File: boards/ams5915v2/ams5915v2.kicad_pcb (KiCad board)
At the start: 2 copper layers, 17.8 x 53.3 mm, 17 parts, among them J1 Conn_01x04, U1 MAX4995A, U2 TLV73333PDBVR, U3 AMS5915, U4 AMS5915

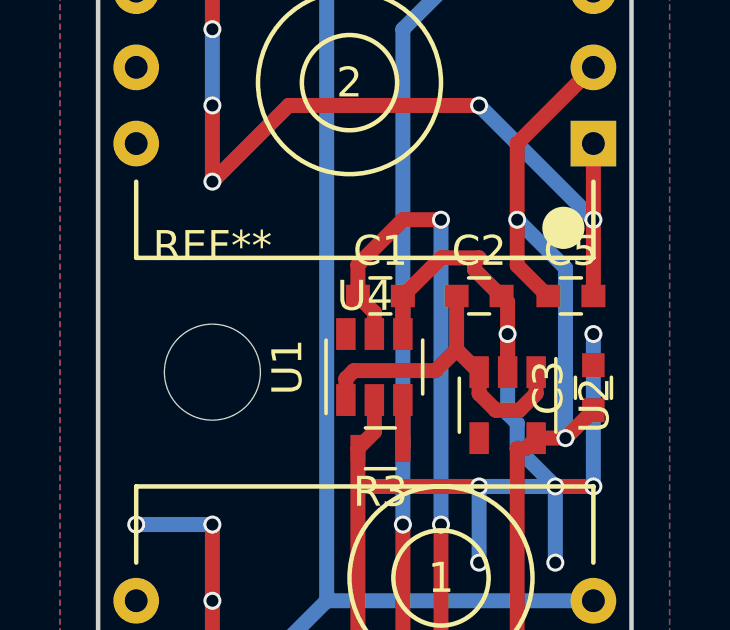
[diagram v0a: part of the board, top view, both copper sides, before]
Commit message: ams5915v2: fixed permanently off max4995
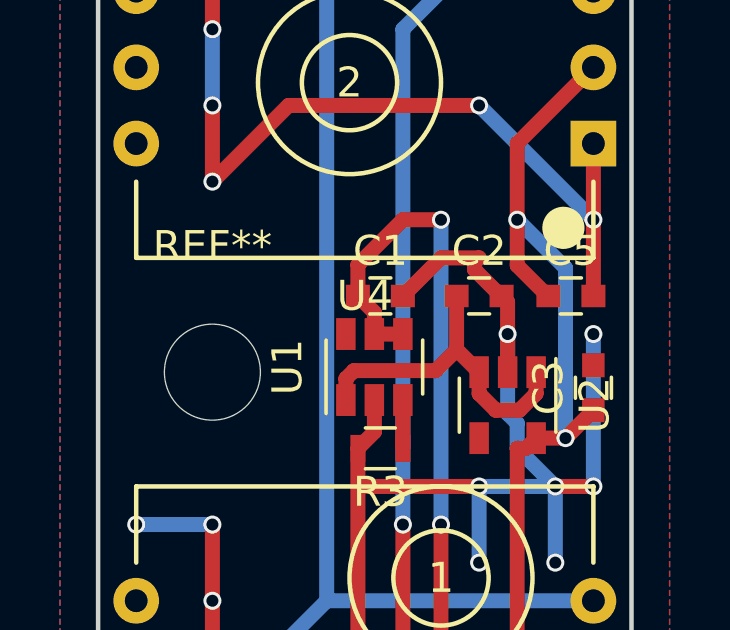
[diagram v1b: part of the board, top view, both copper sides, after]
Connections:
- U1 pad 4: /GND -> /5v
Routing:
- net /GND: track 156.6 -> 155.3 mm
- net /5v: track 36.2 -> 37.1 mm
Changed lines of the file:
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@@
       (net 7 "Net-(R3-Pad1)"))
     (pad 4 smd rect (at 1.1 0.95 90) (size 1.06 0.65) (layers F.Cu F.Paste F.Mask)
-      (net 1 /GND))
+      (net 2 /5v))
     (pad 6 smd rect (at 1.1 -0.95 90) (size 1.06 0.65) (layers F.Cu F.Paste F.Mask)
       (net 8 "Net-(U1-Pad6)"))
@@
   (segment (start 157.33 81.675) (end 158.205 82.55) (width 0.5) (layer F.Cu) (net 1))
   (segment (start 158.205 82.55) (end 158.23 82.55) (width 0.5) (layer F.Cu) (net 1))
-  (segment (start 154.94 82.55) (end 154.94 83.82) (width 0.5) (layer F.Cu) (net 1))
   (segment (start 152.4 95.25) (end 153.67 96.52) (width 0.5) (layer B.Cu) (net 1))
   (segment (start 153.67 96.52) (end 158.75 96.52) (width 0.5) (layer B.Cu) (net 1))
@@
   (segment (start 153.44 87.63) (end 153.99 87.08) (width 0.5) (layer F.Cu) (net 1))
   (segment (start 153.99 87.08) (end 153.99 86.02) (width 0.5) (layer F.Cu) (net 1))
+  (segment (start 153.99 83.82) (end 154.94 83.82) (width 0.5) (layer F.Cu) (net 2))
   (segment (start 156.21 80.01) (end 154.94 80.01) (width 0.5) (layer F.Cu) (net 2))
   (segment (start 154.94 80.01) (end 153.44 81.51) (width 0.5) (layer F.Cu) (net 2))

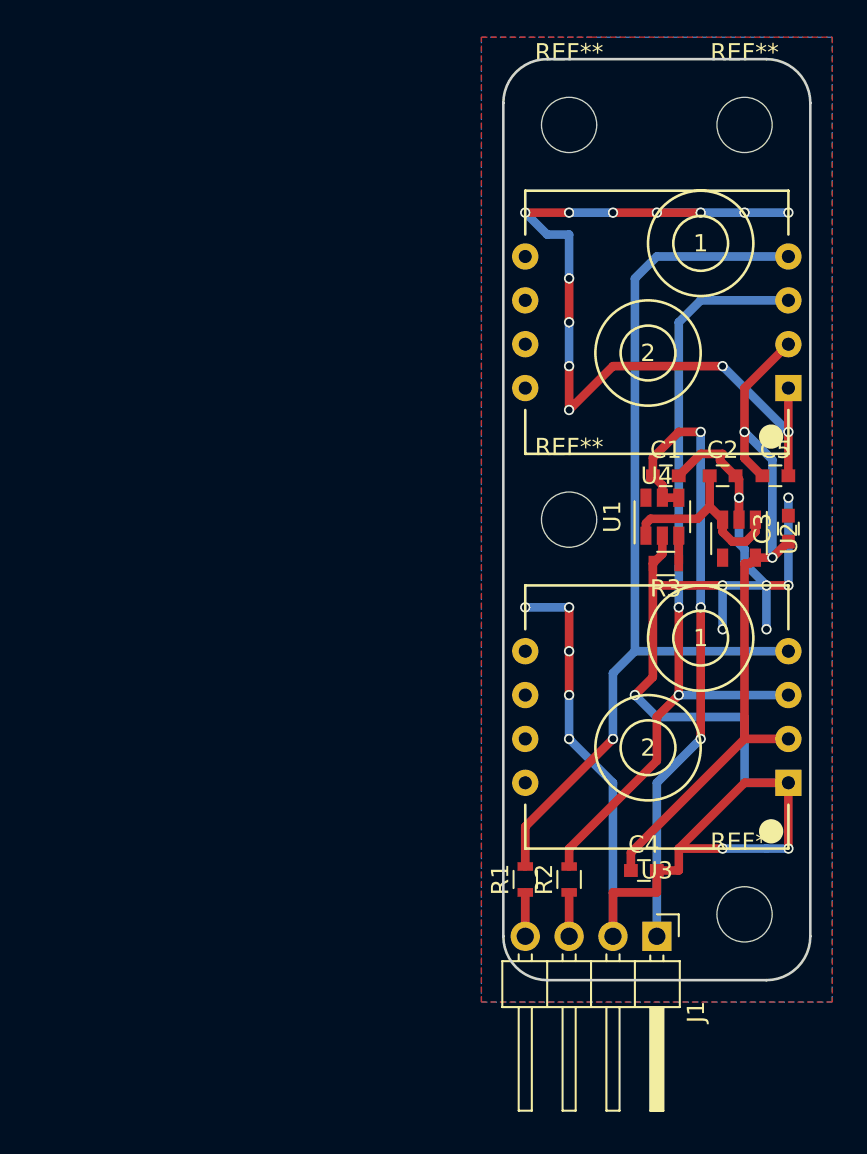
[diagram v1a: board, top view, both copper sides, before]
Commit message: ams5915x2: complete redesign. using leds to signal power, fault and 3v3. added pullup on fault line, fixed missing libs, fixed believed short
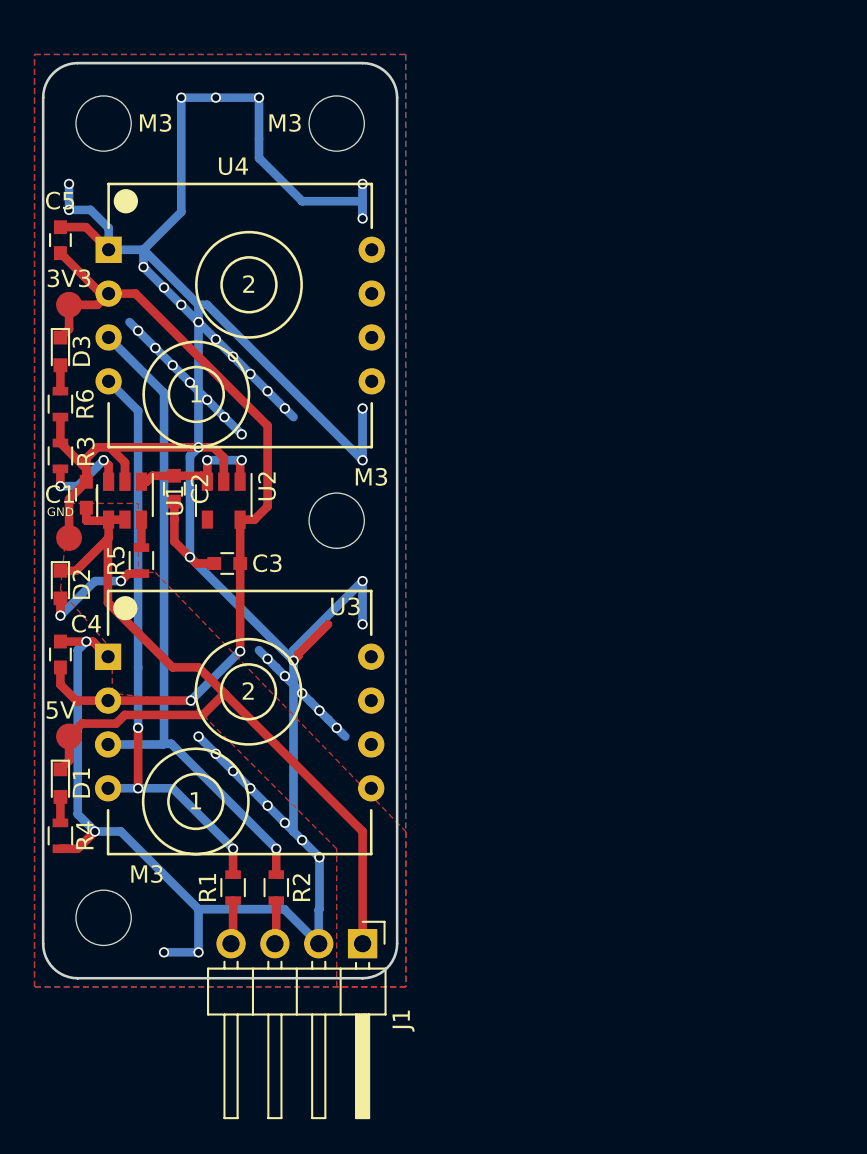
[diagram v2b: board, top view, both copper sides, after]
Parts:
- added 3V3: 3v3, Measurement_Points:Measurement_Point_Round-SMD-Pad_Small, F.Cu at (119.6, 72.7)
- added 5V: 5v, Measurement_Points:Measurement_Point_Round-SMD-Pad_Small, F.Cu at (119.6, 97.7)
- added D1: LED, LEDs:LED_0603, F.Cu at (119.1, 100.3)
- added D2: LED, LEDs:LED_0603, F.Cu at (119.1, 88.8)
- added D3: LED, LEDs:LED_0603, F.Cu at (119.1, 75.3)
- added GND: GND, Measurement_Points:Measurement_Point_Round-SMD-Pad_Small, F.Cu at (119.6, 86.2)
- added R4: R, Resistors_SMD:R_0603, F.Cu at (119.1, 103.4)
- added R5: R, Resistors_SMD:R_0603, F.Cu at (123.8, 87.5)
- added R6: R, Resistors_SMD:R_0603, F.Cu at (119.1, 78.4)
- moved C5 43.6 mm to (119.1, 68.9), turned to 90 degrees
- moved U4 42.4 mm to (121.9, 65.7), turned to 270 degrees
- moved U3 42.1 mm to (121.9, 89.2), turned to 270 degrees
- moved M3 37.1 mm to (121.6, 108.2)
- moved C4 36.0 mm to (119.1, 92.9), turned to 90 degrees
- moved R3 35.6 mm to (119.1, 81.4), turned to 90 degrees
- moved C1 33.6 mm to (120.6, 83.7), turned to 90 degrees
- moved C3 32.6 mm to (128.8, 87.6), turned to 180 degrees
- moved C2 31.8 mm to (125.7, 83.3), turned to 270 degrees
- moved U1 31.1 mm to (122.9, 84.0), turned to 270 degrees
- moved U2 29.9 mm to (128.6, 84.0)
- moved M3 27.0 mm to (121.6, 62.1)
- moved M3 23.6 mm to (135.1, 62.1)
- moved J1 17.0 mm to (136.6, 109.7)
- moved R2 17.0 mm to (131.6, 106.4)
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- renumbered REF** to M3
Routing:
- net /GND: track 155.3 -> 213.2 mm, vias 28 -> 47
- net Net-(R1-Pad2): track 55.0 -> 34.5 mm, vias 1 -> 3
- net /5v: track 37.1 -> 50.3 mm, vias 3 -> 0
- net Net-(R2-Pad2): track 47.4 -> 38.6 mm, vias 2 -> 1
- net Net-(D2-Pad2): track 0.00 -> 6.70 mm, vias 0 -> 2
- net /3v3: track 43.2 -> 48.1 mm
- net Net-(R3-Pad1): track 1.61 -> 5.48 mm, vias 0 -> 2
- net /5vSWITCHED: track 11.4 -> 8.62 mm, vias 0 -> 2
- net Net-(R5-Pad2): track 0.00 -> 1.62 mm
- net Net-(D3-Pad2): track 0.00 -> 1.50 mm
- net Net-(D1-Pad2): track 0.00 -> 1.50 mm
- added copper zone on F.Cu, net /5v
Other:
- board size 17.8 x 53.3 mm -> 20.5 x 53 mm

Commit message: ams5915x2: temp save
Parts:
- removed 3V3: 3v3, Measurement_Points:Measurement_Point_Round-SMD-Pad_Small
- removed 5V: 5v, Measurement_Points:Measurement_Point_Round-SMD-Pad_Small
- removed GND: GND, Measurement_Points:Measurement_Point_Round-SMD-Pad_Small
- removed M3 (x4): MountingHole_3.2mm_M3, Mounting_Holes:MountingHole_3.2mm_M3
- added C6: 100n, Capacitors_SMD:C_0603, F.Cu at (177.5, 82.0)
- added C7: 1u, Capacitors_SMD:C_0805, F.Cu at (185.5, 119.0)
- added C8: 1u, Capacitors_SMD:C_0805, F.Cu at (185.5, 96.5)
- added D4: LED_P2, LEDs:LED_0603, F.Cu at (177.5, 91.8)
- added R7: 400k, Resistors_SMD:R_0603, F.Cu at (184.2, 93.5)
- added R8: 2k7, Resistors_SMD:R_0603, F.Cu at (177.5, 94.8)
- added REF**: MountingHole_3.2mm_M3, Mounting_Holes:MountingHole_3.2mm_M3, F.Cu at (192.5, 96.0)
- added REF**: MountingHole_3.2mm_M3, Mounting_Holes:MountingHole_3.2mm_M3, F.Cu at (192.5, 121.5)
- added REF**: MountingHole_3.2mm_M3, Mounting_Holes:MountingHole_3.2mm_M3, F.Cu at (182.5, 73.0)
- added TP1: 5v, Measurement_Points:Measurement_Point_Round-SMD-Pad_Small, F.Cu at (141.0, 105.0)
- added TP2: GND, Measurement_Points:Measurement_Point_Round-SMD-Pad_Small, F.Cu at (141.0, 109.0)
- added TP3: 3v3, Measurement_Points:Measurement_Point_Round-SMD-Pad_Small, F.Cu at (141.0, 113.5)
- added U5: AMS5915, kicad-footprints-rchojetzki:AMS_5915-XXXX-D_differential_pressure_sensor, F.Cu at (179.8, 77.1)
- C1: footprint Capacitors_SMD:C_0603 -> Capacitors_SMD:C_0805
- C2: value 100n -> 10u; footprint Capacitors_SMD:C_0603 -> Capacitors_SMD:C_1206
- C3: value 1u -> 100n
- D1: value LED -> LED_5v
- D2: value LED -> LED_3v3
- D3: value LED -> LED_P1
- R3: value 300k -> 4k7
- R4, R6: value R -> 2k7
- R5: value R -> 400k
- U1: value MAX4995A -> TLV73333PDBVR; footprint TO_SOT_Packages_SMD:SOT-23-6 -> TO_SOT_Packages_SMD:SOT-23-5
- U2: value TLV73333PDBVR -> MAX4995A; footprint TO_SOT_Packages_SMD:SOT-23-5 -> TO_SOT_Packages_SMD:SOT-23-6
- U4: value AMS5915 -> MAX4995A; footprint kicad-footprints-rchojetzki:AMS_5915-XXXX-D_differential_pressure_sensor -> TO_SOT_Packages_SMD:SOT-23-6
- moved R4 73.9 mm to (187.8, 76.0), turned to 180 degrees
- moved U1 70.5 mm to (192.4, 72.0), turned to 180 degrees
- moved D3 70.3 mm to (177.5, 114.5), turned to 90 degrees
- moved R6 70.3 mm to (177.5, 117.5)
- moved R3 69.3 mm to (188.0, 74.0), turned to 0 degrees
- moved C1 68.4 mm to (188.0, 72.0), turned to 0 degrees
- moved C2 67.2 mm to (192.5, 75.5), turned to 0 degrees
- moved U4 66.9 mm to (181.6, 96.0), turned to 180 degrees
- moved R5 66.8 mm to (184.2, 116.0), turned to 0 degrees
- moved C5 66.8 mm to (181.2, 93.5), turned to 0 degrees
- moved D1 64.1 mm to (177.5, 73.8), turned to 90 degrees
- moved U2 63.5 mm to (181.9, 118.5), turned to 180 degrees
- moved C3 59.6 mm to (181.2, 116.0), turned to 0 degrees
- moved C4 59.5 mm to (177.5, 104.5)
- moved D2 59.3 mm to (177.5, 78.5), turned to 90 degrees
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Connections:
- C2 pad 1: /5vSWITCHED -> /3v3
- C4 pad 1: /3v3 -> Net-(C4-Pad1)
- D1 pad 1: /5v -> Net-(D1-Pad1)
- D1 pad 2: Net-(D1-Pad2) -> /5v
- D2 pad 1: /5v -> /GND
- D3 pad 1: /3v3 -> Net-(D3-Pad1)
- D3 pad 2: Net-(D3-Pad2) -> /3v3
- R3 pad 1: Net-(R3-Pad1) -> Net-(D1-Pad1)
- R4 pad 1: Net-(D1-Pad2) -> /3v3
- R4 pad 2: /GND -> Net-(D2-Pad2)
- R5 pad 1: Net-(D2-Pad2) -> /GND
- R6 pad 1: Net-(D3-Pad2) -> Net-(D3-Pad1)
- R6 pad 2: /GND -> Net-(R6-Pad2)
- U1 pad 1: /5vSWITCHED -> /5v
- U1 pad 3: Net-(R3-Pad1) -> /5v
- U1 pad 4: /5v -> Net-(U1-Pad4)
- U1 pad 5: /5v -> /3v3
- U2 pad 1: /5vSWITCHED -> Net-(C4-Pad1)
- U2 pad 3: /5vSWITCHED -> Net-(R5-Pad2)
- U2 pad 4: Net-(U2-Pad4) -> /3v3
- U3 pad 2: /3v3 -> Net-(C4-Pad1)
- U4 pad 1: /GND -> Net-(C6-Pad1)
- U4 pad 2: /3v3 -> /GND
- U4 pad 3: Net-(R2-Pad2) -> Net-(R7-Pad2)
- U4 pad 4: Net-(R1-Pad2) -> /3v3
- U4 pad 5: Net-(U4-Pad5) -> /3v3
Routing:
- net /GND: track 213.2 -> 58.4 mm, vias 47 -> 2
- net /3v3: track 48.1 -> 75.5 mm, vias 2 -> 3
- net Net-(C6-Pad1): track 0.00 -> 23.1 mm
- net Net-(C4-Pad1): track 0.00 -> 22.7 mm
- net /5v: track 50.3 -> 72.2 mm, vias 0 -> 3
- net Net-(D1-Pad1): track 0.00 -> 12.0 mm
- net /5vSWITCHED: track 8.62 -> 0.00 mm, vias 2 -> 0
- net Net-(R3-Pad1): track 5.48 -> 0.00 mm, vias 2 -> 0
- net Net-(R1-Pad2): track 34.5 -> 39.0 mm, vias 3 -> 2
- net Net-(R8-Pad2): track 0.00 -> 3.87 mm
- net Net-(R6-Pad2): track 0.00 -> 3.82 mm
- net Net-(D2-Pad2): track 6.70 -> 10.5 mm, vias 2 -> 0
- net Net-(R7-Pad2): track 0.00 -> 3.54 mm
- net Net-(R5-Pad2): track 1.62 -> 3.28 mm
- net Net-(D3-Pad2): track 1.50 -> 0.00 mm
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- added copper zone on B.Cu, net /3v3
- added copper zone on B.Cu, net /5v
- removed copper zone on F.Cu, net /5v
- removed copper zone on F.Cu, net /GND
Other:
- board size 20.5 x 53 mm -> 20 x 56.5 mm
- net class Default: trace_width 0.5 -> 0.6
- rule pad_to_mask_clearance: 0.2 -> 0

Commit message: ams5915x2: board completed in v3, labels are still missing
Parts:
- moved TP1 50.2 mm to (178.0, 71.0)
- moved TP3 45.1 mm to (177.5, 87.0)
- moved TP2 38.0 mm to (178.0, 100.5)
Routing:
- net /GND: track 58.4 -> 65.8 mm, vias 2 -> 3
- net /3v3: track 75.5 -> 78.0 mm
- net /5v: track 72.2 -> 73.9 mm, vias 3 -> 4
- added copper zone on F.Cu, net /GND
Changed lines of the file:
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@@
   (general
     (links 54)
-    (no_connects 9)
-    (area 176.449999 68.949999 196.550001 122.550001)
+    (no_connects 0)
+    (area 176.449999 68.949999 196.550001 125.550001)
     (thickness 1.6)
     (drawings 8)
-    (tracks 159)
+    (tracks 169)
     (zones 0)
     (modules 32)
@@
   )
   (module Measurement_Points:Measurement_Point_Round-SMD-Pad_Small (layer F.Cu)
-    (at 141 105)
+    (at 178 71)
     (descr "Mesurement Point, Round, SMD Pad, DM 1.5mm,")
     (tags "Mesurement Point Round SMD Pad 1.5mm")
@@
   )
   (module Measurement_Points:Measurement_Point_Round-SMD-Pad_Small (layer F.Cu)
-    (at 141 109)
+    (at 178 100.5)
     (descr "Mesurement Point, Round, SMD Pad, DM 1.5mm,")
     (tags "Mesurement Point Round SMD Pad 1.5mm")
@@
   )
   (module Measurement_Points:Measurement_Point_Round-SMD-Pad_Small (layer F.Cu)
-    (at 141 113.5)
+    (at 177.5 87)
     (descr "Mesurement Point, Round, SMD Pad, DM 1.5mm,")
     (tags "Mesurement Point Round SMD Pad 1.5mm")
@@
   (gr_line (start 196.5 71) (end 196.5 123.5) (layer Edge.Cuts) (width 0.1))
   (gr_line (start 176.5 123.5) (end 176.5 71) (layer Edge.Cuts) (width 0.1))
+  (segment (start 185 96) (end 185 100) (width 0.6) (layer B.Cu) (net 1))
+  (via (at 185 100) (size 0.6) (drill 0.4) (layers F.Cu B.Cu) (net 1))
+  (segment (start 185 100) (end 185 117.5) (width 0.6) (layer B.Cu) (net 1))
+  (segment (start 183.250001 99.750001) (end 183.5 100) (width 0.6) (layer F.Cu) (net 1))
+  (segment (start 183.5 100) (end 185 100) (width 0.6) (layer F.Cu) (net 1))
+  (segment (start 178 100.5) (end 178.749999 99.750001) (width 0.6) (layer F.Cu) (net 1))
+  (segment (start 178.749999 99.750001) (end 183.250001 99.750001) (width 0.6) (layer F.Cu) (net 1))
   (segment (start 185.5 118) (end 184.5 119) (width 0.6) (layer F.Cu) (net 1))
-  (segment (start 185 96) (end 185 117.5) (width 0.6) (layer B.Cu) (net 1))
   (segment (start 185 117.5) (end 185.5 118) (width 0.6) (layer B.Cu) (net 1))
   (via (at 185.5 118) (size 0.6) (drill 0.4) (layers F.Cu B.Cu) (net 1))
@@
   (segment (start 181.87 118.55) (end 183 118.55) (width 0.6) (layer F.Cu) (net 1))
   (segment (start 183.5 116) (end 182 116) (width 0.6) (layer F.Cu) (net 1))
+  (segment (start 177.5 73) (end 177.5 72) (width 0.6) (layer F.Cu) (net 2))
+  (segment (start 177.5 72) (end 178 71.5) (width 0.6) (layer F.Cu) (net 2))
+  (via (at 178 71.5) (size 0.6) (drill 0.4) (layers F.Cu B.Cu) (net 2))
   (segment (start 192.5 74) (end 192.5 91.5) (width 0.6) (layer B.Cu) (net 2))
   (segment (start 192.5 91.5) (end 195.5 94.5) (width 0.6) (layer B.Cu) (net 2))
@@
   (via (at 187 70.5) (size 0.6) (drill 0.4) (layers F.Cu B.Cu) (net 2))
   (segment (start 187 72) (end 187 70.5) (width 0.6) (layer F.Cu) (net 2))
+  (segment (start 177.5 89.5) (end 177.5 87) (width 0.6) (layer F.Cu) (net 3))
   (segment (start 188.5 76) (end 189.5 76) (width 0.6) (layer F.Cu) (net 3))
   (segment (start 189.5 76) (end 190.5 76) (width 0.6) (layer F.Cu) (net 3))
@@
       )
     )
+  )
+  (zone (net 1) (net_name /GND) (layer F.Cu) (hatch edge 0.508)
+    (priority 3)
+    (connect_pads (clearance 0.508))
+    (min_thickness 0.254)
+    (fill yes (arc_segments 16) (thermal_gap 0.508) (thermal_bridge_width 0.508))
+    (polygon
+      (pts
+        (xy 176 68.5) (xy 197 68.5) (xy 197 126) (xy 176 126)
+      )
+    )

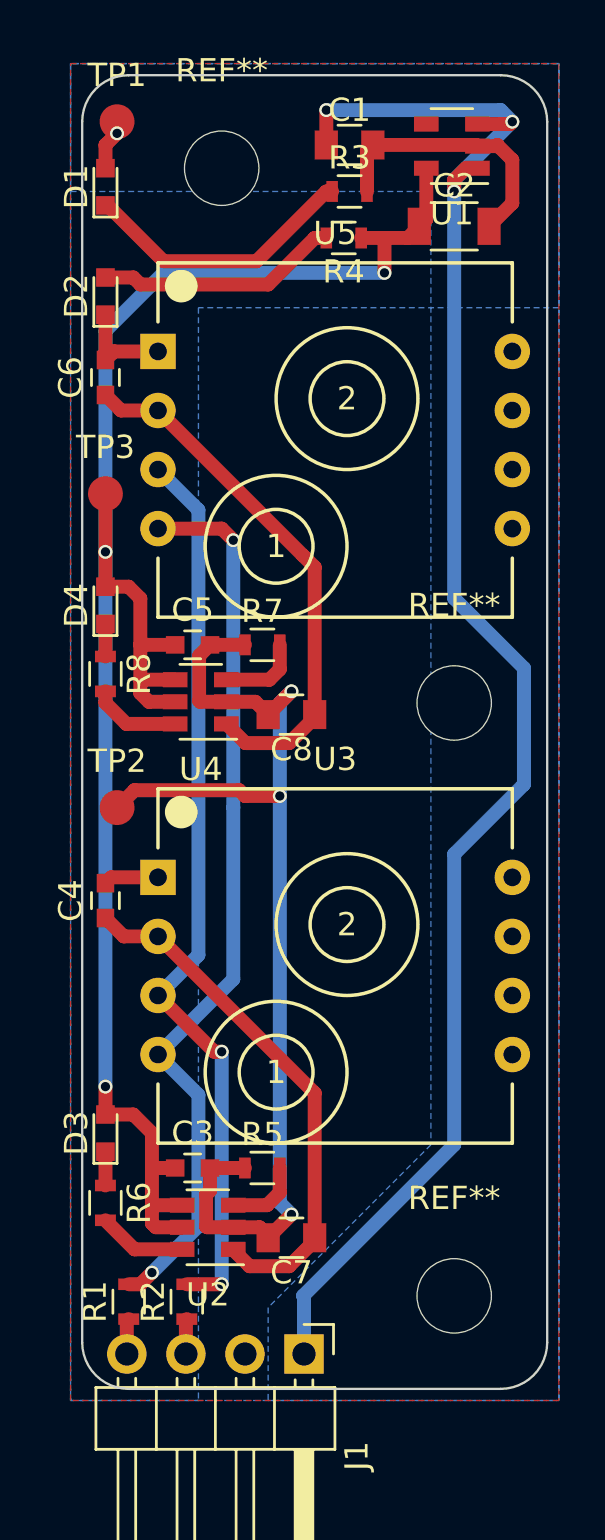
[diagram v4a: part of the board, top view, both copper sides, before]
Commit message: ams5915x2: placed labels
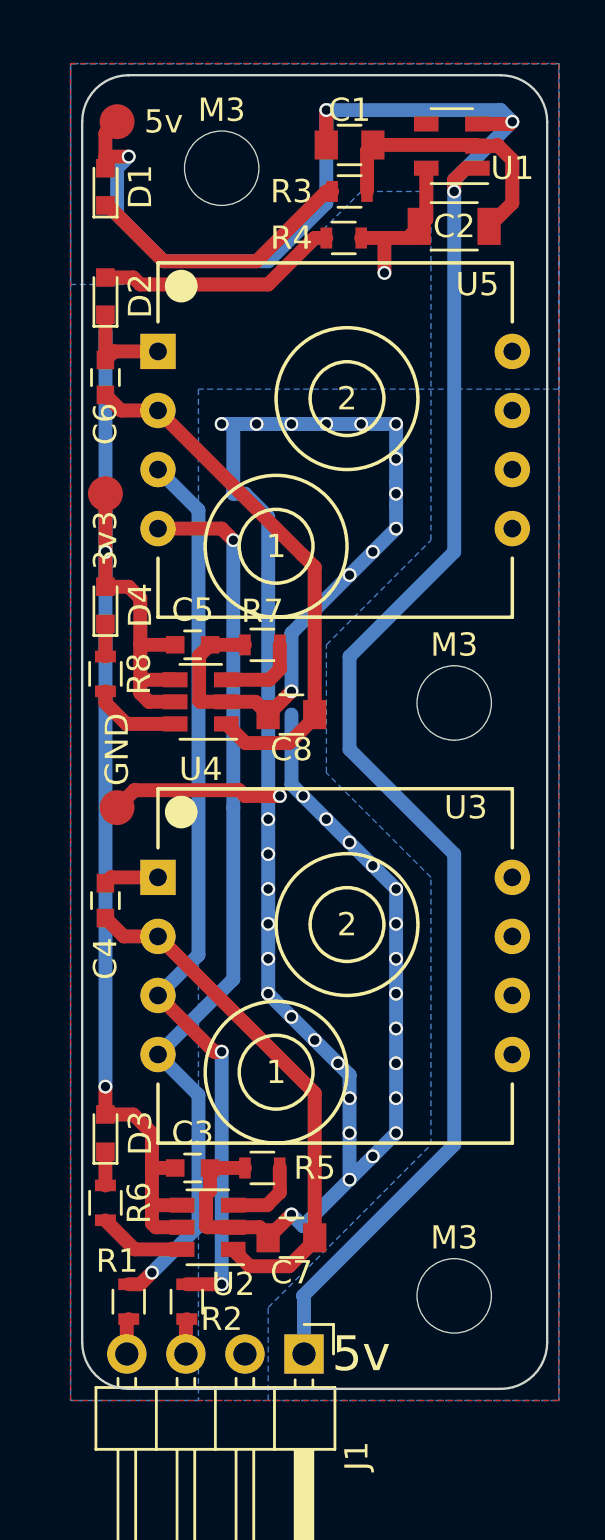
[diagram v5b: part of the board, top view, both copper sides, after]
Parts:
- renumbered TP3 to 3v3, TP1 to 5v, TP2 to GND, REF** to M3
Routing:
- net /GND: track 65.8 -> 126.4 mm, vias 3 -> 39
- net /5v: track 73.9 -> 94.2 mm
- net /3v3: track 78.0 -> 64.9 mm
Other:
- board text added: "5v"
